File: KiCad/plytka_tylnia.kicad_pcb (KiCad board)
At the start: 2 copper layers, 150 x 140 mm, 80 parts, among them J1 CONN_01X04, J2 CONN_01X04, J3 CONN_01X04, J4 CONN_01X04, J5 CONN_01X04, J6 CONN_01X04, J7 PIN10, J8 CONN_01X04, J9 CONN_01X04, P1 USB_OTG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

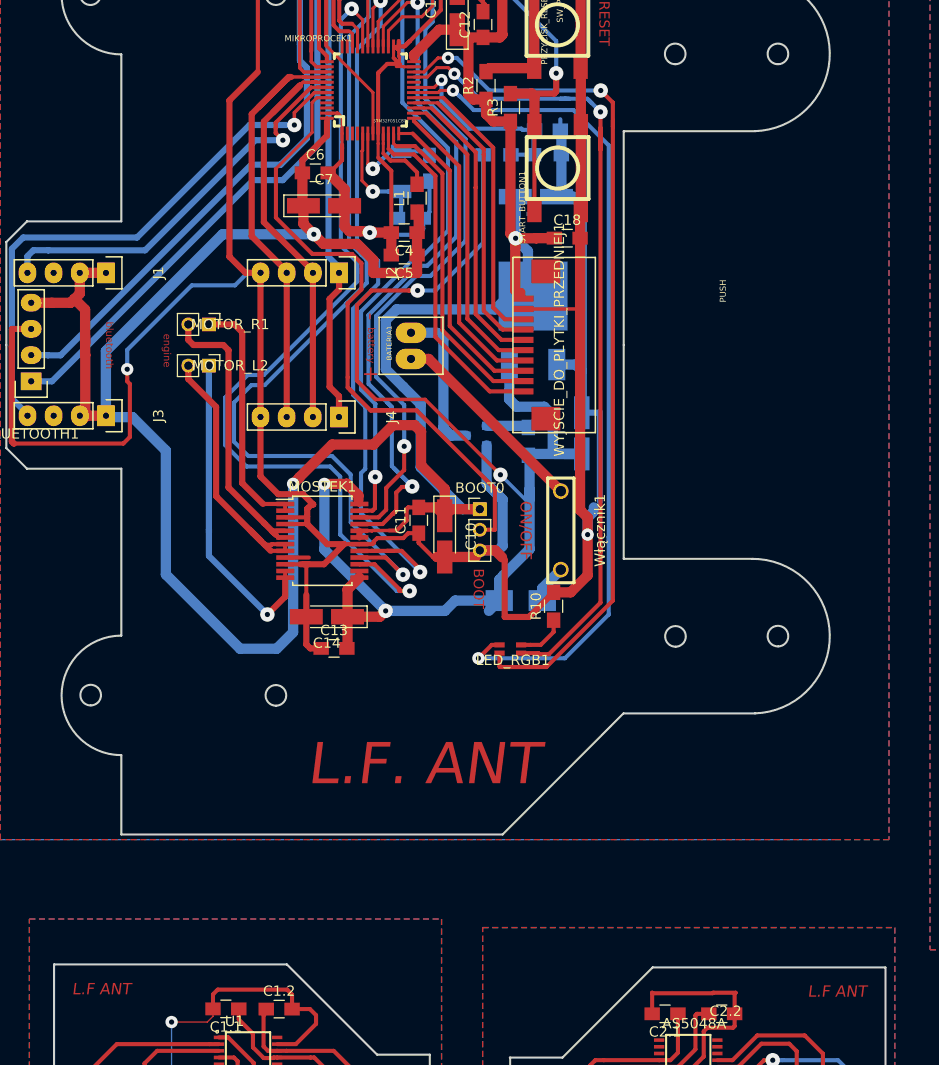
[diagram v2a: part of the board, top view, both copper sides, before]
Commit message: dodanie mocowania magnesow w inventorze
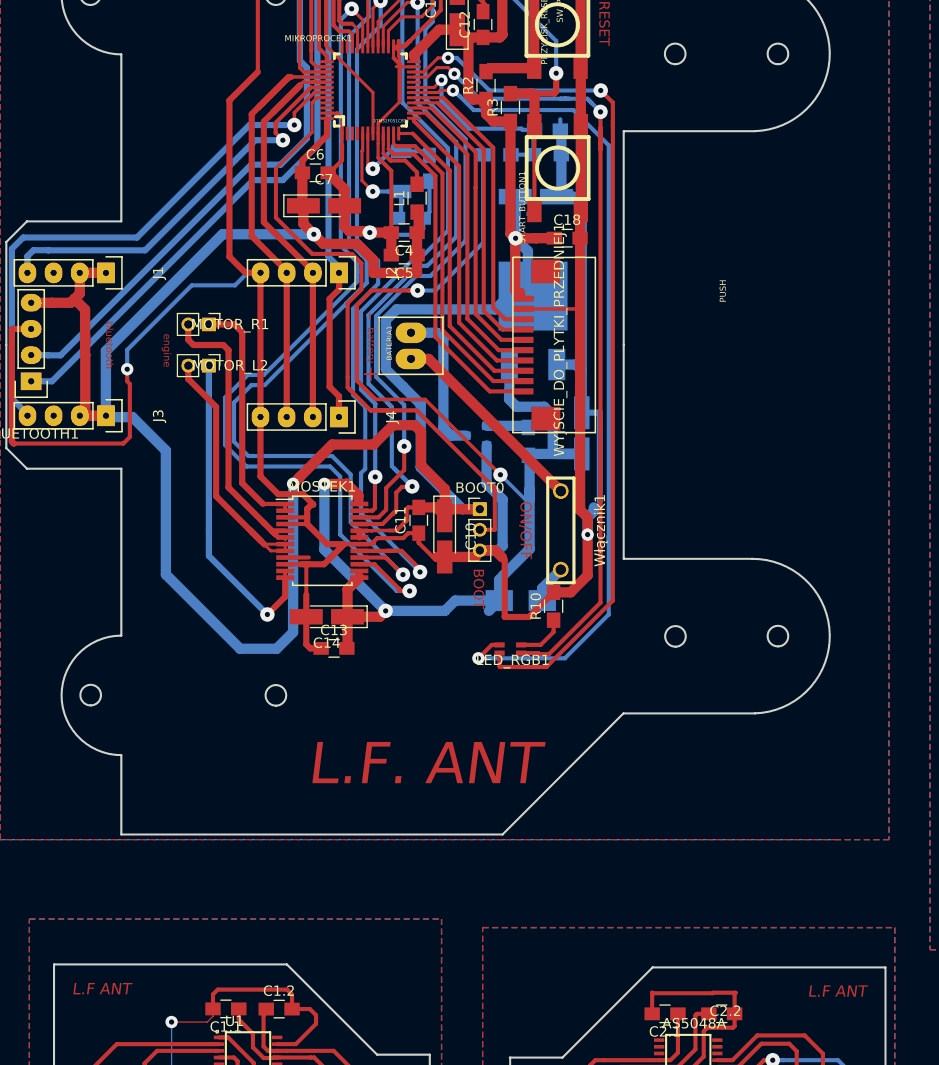
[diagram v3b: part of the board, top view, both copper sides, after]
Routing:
- net GND: track 499.5 -> 498.8 mm
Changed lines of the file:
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@@
   )
   (setup
-    (last_trace_width 0.4)
+    (last_trace_width 0.3)
     (user_trace_width 0.2)
     (user_trace_width 0.3)
@@
     (effects (font (size 1 1) (thickness 0.2)))
   )
-  (gr_text "L.F ANT" (at 150.21484 162.73236 360) (layer F.Cu)
+  (gr_text "L.F ANT" (at 150.21484 162.73236) (layer F.Cu)
     (effects (font (size 1.1 1.1) (thickness 0.2) italic))
   )
-  (gr_text "L.F ANT" (at 78.825 162.5 360) (layer F.Cu)
+  (gr_text "L.F ANT" (at 78.825 162.5) (layer F.Cu)
     (effects (font (size 1.1 1.1) (thickness 0.2) italic))
   )
@@
     (effects (font (size 1.5 1.5) (thickness 0.3) italic))
   )
-  (gr_text "L.F. ANT" (at 110.078 140.668 360) (layer F.Cu)
+  (gr_text "L.F. ANT" (at 110.078 140.668) (layer F.Cu)
     (effects (font (size 4 4) (thickness 0.9) italic))
   )
@@
   (segment (start 98.76 79.95) (end 96.21 82.5) (width 0.6) (layer B.Cu) (net 6))
   (segment (start 93.36 82.5) (end 74.86 101) (width 0.6) (layer B.Cu) (net 6))
+  (segment (start 105.6693 79.47402) (end 105.6693 78.49965) (width 0.3) (layer F.Cu) (net 7))
+  (segment (start 105.6693 78.49965) (end 107.75 76.41895) (width 0.3) (layer F.Cu) (net 7))
+  (segment (start 107.75 76.41895) (end 107.75 76.31895) (width 0.3) (layer F.Cu) (net 7))
+  (segment (start 107.75 76.31895) (end 107.75 72.71825) (width 0.4) (layer F.Cu) (net 7))
+  (segment (start 107.75 72.71825) (end 107.1679 72.13615) (width 0.4) (layer F.Cu) (net 7))
   (segment (start 103.85 119.325) (end 102.375 119.325) (width 0.4) (layer F.Cu) (net 7))
   (segment (start 98.785 115.89) (end 98.785 116.65) (width 0.6) (layer F.Cu) (net 7))
@@
   (segment (start 111.39 120.57) (end 112.13 120.57) (width 1) (layer F.Cu) (net 7))
   (segment (start 115.15 120.57) (end 111.39 120.57) (width 1) (layer F.Cu) (net 7))
-  (segment (start 105.76825 73.5) (end 106.55 72.71825) (width 0.4) (layer F.Cu) (net 7))
-  (segment (start 105.6693 79.47402) (end 105.6693 73.59895) (width 0.4) (layer F.Cu) (net 7))
-  (segment (start 105.6693 73.59895) (end 105.76825 73.5) (width 0.4) (layer F.Cu) (net 7))
-  (segment (start 107.75 72.71825) (end 107.1679 72.13615) (width 0.4) (layer F.Cu) (net 7))
-  (segment (start 106.55 72.71825) (end 107.75 72.71825) (width 0.4) (layer F.Cu) (net 7))
   (segment (start 102.42 86.49) (end 102.42 84.89) (width 1) (layer F.Cu) (net 7))
   (segment (start 102.42 84.89) (end 100.82 83.29) (width 1) (layer F.Cu) (net 7))
@@
   (segment (start 92.48 113.405) (end 94.5 115.425) (width 0.6) (layer F.Cu) (net 36))
   (segment (start 96.65 115.425) (end 96.65 116.075) (width 0.4) (layer F.Cu) (net 36))
+  (segment (start 96.65 118.675) (end 96.65 118.9) (width 0.3) (layer F.Cu) (net 37))
   (segment (start 96.65 118.675) (end 96 118.675) (width 0.4) (layer F.Cu) (net 37))
   (segment (start 96 118.675) (end 95.4 118.075) (width 0.4) (layer F.Cu) (net 37))
@@
   (segment (start 95.65 118.025) (end 95.5 118.175) (width 0.4) (layer F.Cu) (net 37))
   (segment (start 96.65 118.025) (end 95.65 118.025) (width 0.4) (layer F.Cu) (net 37))
-  (segment (start 95.25 119.975) (end 94.65 119.375) (width 0.6) (layer F.Cu) (net 38))
+  (segment (start 96.65 119.975) (end 96.65 119.325) (width 0.3) (layer F.Cu) (net 38))
+  (segment (start 96.65 119.975) (end 95.25 119.975) (width 0.3) (layer F.Cu) (net 38))
+  (segment (start 95.25 119.975) (end 94.65 119.375) (width 0.3) (layer F.Cu) (net 38))
+  (segment (start 96.65 119.325) (end 94.7 119.325) (width 0.3) (layer F.Cu) (net 38))
+  (segment (start 94.7 119.325) (end 94.65 119.375) (width 0.3) (layer F.Cu) (net 38))
   (segment (start 94.65 119.375) (end 94.275 119) (width 0.6) (layer F.Cu) (net 38))
-  (segment (start 95.375 119.325) (end 95.325 119.375) (width 0.4) (layer F.Cu) (net 38))
-  (segment (start 96.65 119.325) (end 95.375 119.325) (width 0.4) (layer F.Cu) (net 38))
-  (segment (start 95.325 119.375) (end 94.65 119.375) (width 0.4) (layer F.Cu) (net 38))
-  (segment (start 96.65 119.975) (end 96.65 119.325) (width 0.4) (layer F.Cu) (net 38))
-  (segment (start 96.65 119.975) (end 95.25 119.975) (width 0.4) (layer F.Cu) (net 38))
   (segment (start 87.25 102) (end 87.25 103.3) (width 0.6) (layer F.Cu) (net 38))
   (segment (start 89.95 114.675) (end 93.5 118.225) (width 0.6) (layer F.Cu) (net 38))
@@
     (connect_pads (clearance 0.508))
     (min_thickness 0.254)
-    (fill yes (arc_segments 16) (thermal_gap 0.508) (thermal_bridge_width 0.508))
+    (fill (arc_segments 16) (thermal_gap 0.508) (thermal_bridge_width 0.508))
     (polygon
       (pts
@@
     (connect_pads (clearance 0.508))
     (min_thickness 0.254)
-    (fill yes (arc_segments 16) (thermal_gap 0.508) (thermal_bridge_width 0.508))
+    (fill (arc_segments 16) (thermal_gap 0.508) (thermal_bridge_width 0.508))
     (polygon
       (pts
@@
     (connect_pads (clearance 0.508))
     (min_thickness 0.254)
-    (fill yes (arc_segments 16) (thermal_gap 0.508) (thermal_bridge_width 0.508))
+    (fill (arc_segments 16) (thermal_gap 0.508) (thermal_bridge_width 0.508))
     (polygon
       (pts
@@
     (connect_pads (clearance 0.508))
     (min_thickness 0.254)
-    (fill yes (arc_segments 16) (thermal_gap 0.508) (thermal_bridge_width 0.508))
+    (fill (arc_segments 16) (thermal_gap 0.508) (thermal_bridge_width 0.508))
     (polygon
       (pts
@@
     (connect_pads (clearance 0.508))
     (min_thickness 0.254)
-    (fill yes (arc_segments 16) (thermal_gap 0.508) (thermal_bridge_width 0.508))
+    (fill (arc_segments 16) (thermal_gap 0.508) (thermal_bridge_width 0.508))
     (polygon
       (pts
@@
     (connect_pads (clearance 0.508))
     (min_thickness 0.254)
-    (fill yes (arc_segments 16) (thermal_gap 0.508) (thermal_bridge_width 0.508))
+    (fill (arc_segments 16) (thermal_gap 0.508) (thermal_bridge_width 0.508))
     (polygon
       (pts
@@
     (connect_pads (clearance 0.508))
     (min_thickness 0.254)
-    (fill yes (arc_segments 16) (thermal_gap 0.508) (thermal_bridge_width 0.508))
+    (fill (arc_segments 16) (thermal_gap 0.508) (thermal_bridge_width 0.508))
     (polygon
       (pts
@@
     (connect_pads (clearance 0.508))
     (min_thickness 0.254)
-    (fill yes (arc_segments 16) (thermal_gap 0.508) (thermal_bridge_width 0.508))
+    (fill (arc_segments 16) (thermal_gap 0.508) (thermal_bridge_width 0.508))
     (polygon
       (pts
